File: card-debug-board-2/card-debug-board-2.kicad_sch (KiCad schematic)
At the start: 30 parts, among them J1 2-1734592-0, J2 Conn_01x05, J5 0676430910, J6 629105150521, SW1 PCM13SMTR, SW2 B3F-1000, SW3 CFS-0103TB, SW4 CFS-0103TB, U1 MIC5205-3.3YM5

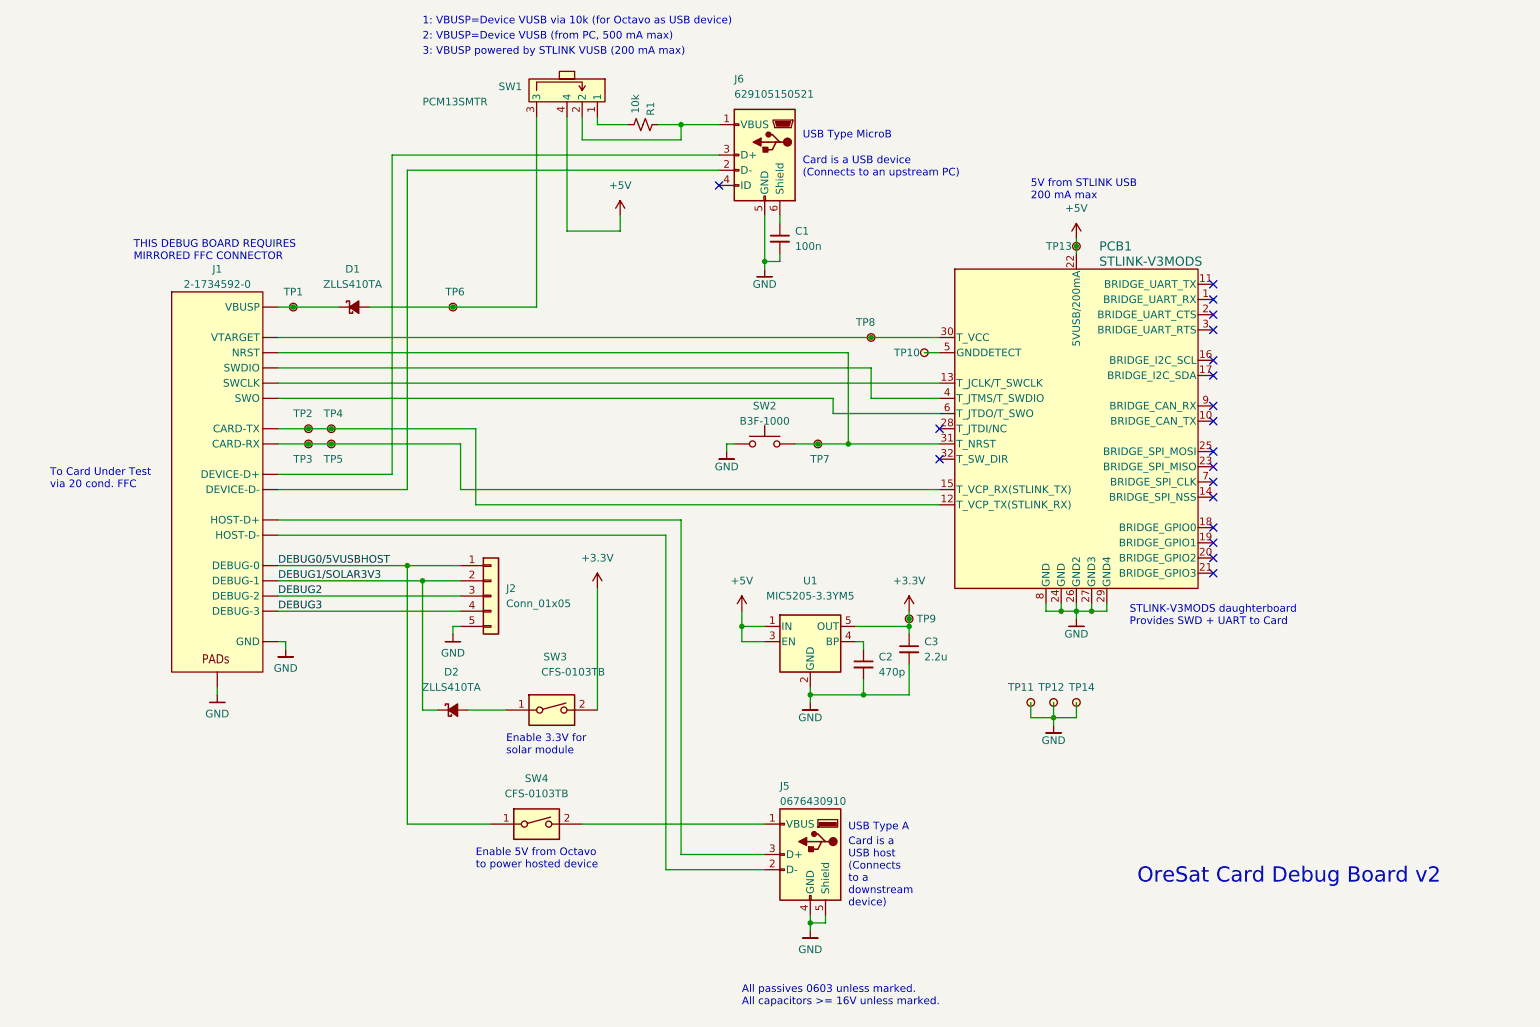
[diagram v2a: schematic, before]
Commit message: Updated .gitignore, silkscreen fix to card-debug-2, file cleanup for flatsat breakout board.
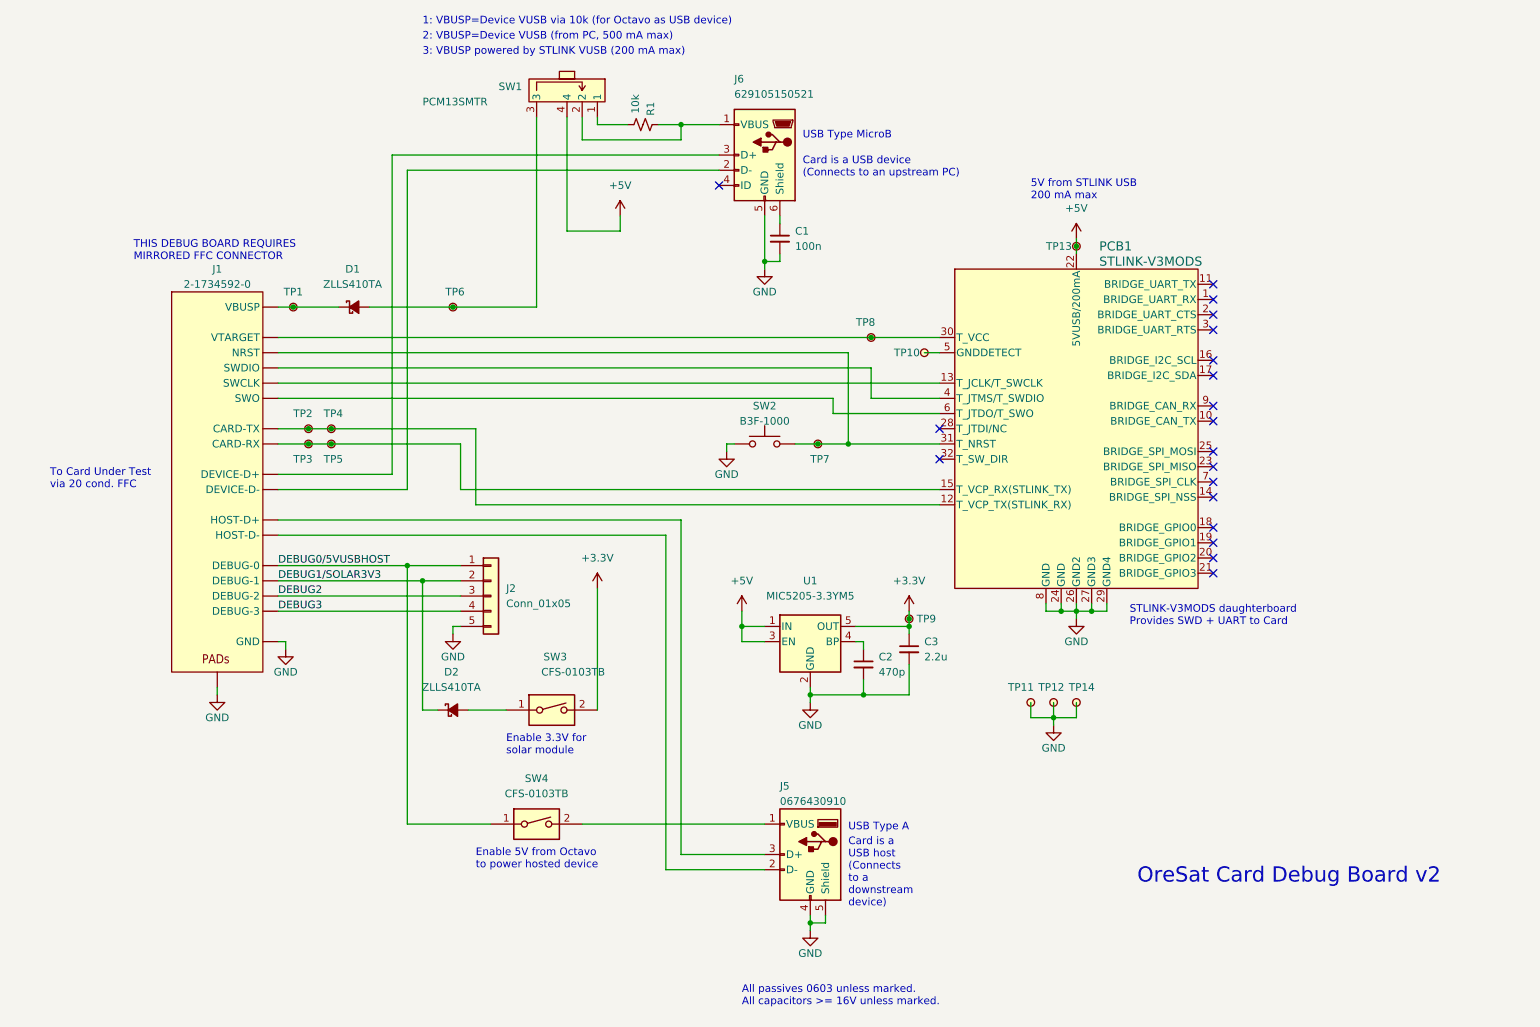
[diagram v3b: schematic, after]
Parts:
- TP1, TP10, TP11, TP12, TP13, TP14, TP2, TP3, TP4, TP5, TP6, TP7, TP8, TP9: now in the parts list

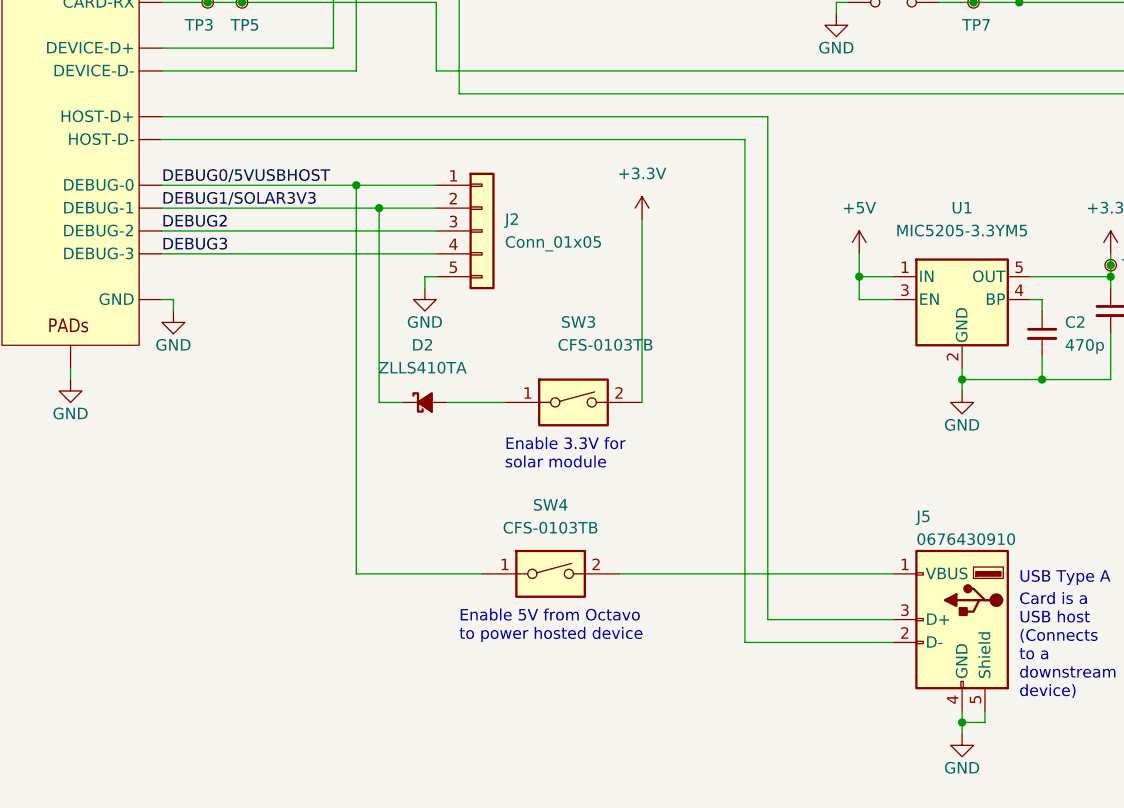
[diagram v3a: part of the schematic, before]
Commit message: Card Debug Board v3
new switch & layout (tracing not finished).
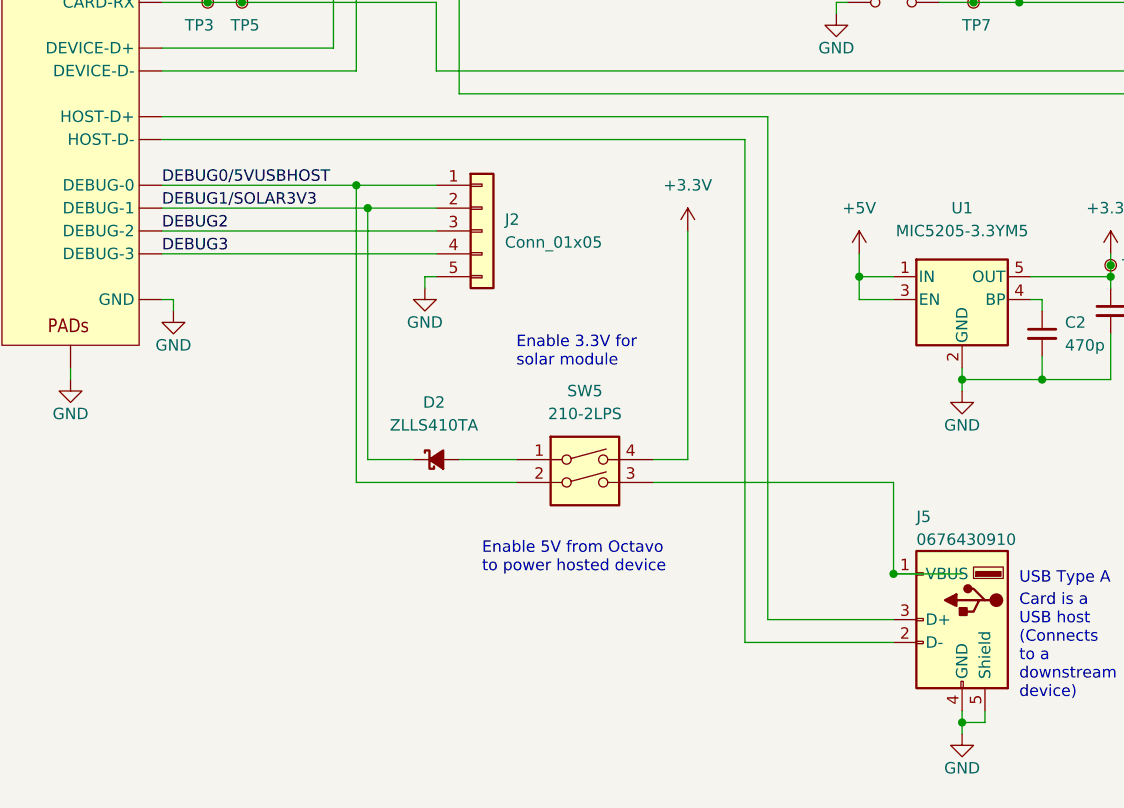
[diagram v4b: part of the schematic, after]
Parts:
- removed SW3, SW4: CFS-0103TB, Button_Switch_SMD:SW_DIP_SPSTx01_Slide_Copal_CHS-01B_W7.62mm_P1.27mm, symbol Switch:SW_DIP_x01
- added SW5: 210-2LPS, Button_Switch_THT:SW_DIP_SPSTx02_Slide_6.7x6.64mm_W7.62mm_P2.54mm_LowProfile, symbol Switch:SW_DIP_x02
- J1: value 2-1734592-0 -> 2-1734592-0
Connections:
- net +3.3V: now also SW5.4
- net DEBUG0/5VUSBHOST: now also SW5.2
- net at D2.2 (A): now also SW5.1
- net at J5.1 (VBUS): now also SW5.3
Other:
- moved on the sheet: D2

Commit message: restore v2 card debug board files
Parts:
- removed SW5: 210-2LPS, Button_Switch_THT:SW_DIP_SPSTx02_Slide_6.7x6.64mm_W7.62mm_P2.54mm_LowProfile, symbol Switch:SW_DIP_x02
- added SW3, SW4: CFS-0103TB, Button_Switch_SMD:SW_DIP_SPSTx01_Slide_Copal_CHS-01B_W7.62mm_P1.27mm, symbol Switch:SW_DIP_x01
- J1: value 2-1734592-0 -> 2-1734592-0
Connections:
- net +3.3V: now also SW3.2
- net DEBUG0/5VUSBHOST: now also SW4.1
- net at D2.2 (A): now also SW3.1
- net at J5.1 (VBUS): now also SW4.2
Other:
- moved on the sheet: D2
